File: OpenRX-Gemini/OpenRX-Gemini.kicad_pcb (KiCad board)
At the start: 6 copper layers, 13.8 x 13.7 mm, 67 parts, among them T1 0900PC16J0042001E, T2 0900PC16J0042001E, U1 ESP32-C3FH4, U10 RFX2401C, U11 SKY13588-460LF, U2 TLV75533PDQNR, U3 TS2306A 240GF MSM 9_C2976675, U4 LR1121IMLTRT, U5 OW7EL89CENUYO3YLC-32M, U6 SKY13588-460LF, U7 RFX2401C, U8 OW7EL89CENUYO3YLC-32M, U9 LR1121IMLTRT, X1 CJ17-400001010B20

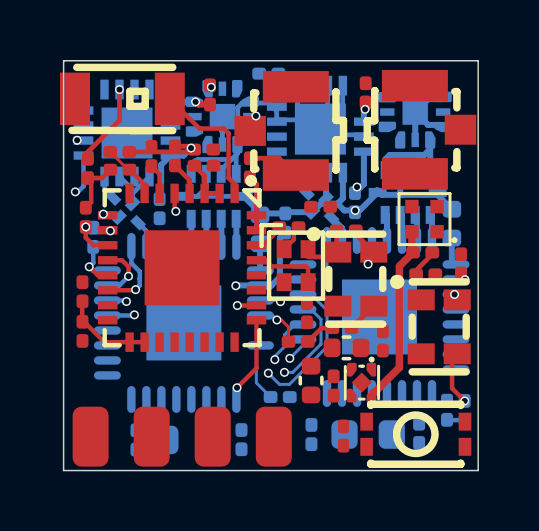
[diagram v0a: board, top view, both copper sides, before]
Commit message: Standardize repo: .gitignore, README, license, remove production from tracking
- Standardize .gitignore to match ecosystem template
- Add license section to README
- Replace LICENSE stub with full CERN-OHL-S-2.0 text
- Remove production/ from git tracking (generated, re-exportable)
- Remove tracked iCloud artifacts (.history 2 files)

Co-Authored-By: Claude Opus 4.6 (1M context) <noreply@anthropic.com>
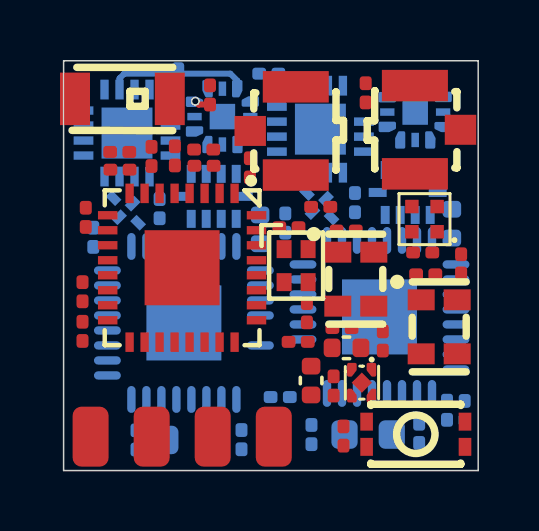
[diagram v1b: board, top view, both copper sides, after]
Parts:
- C16: moved to B.Cu
- moved C16 4.24 mm to (65.3, 45.3)
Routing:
- net GND: track 41.1 -> 0.00 mm, vias 2 -> 0
- net +3V3: track 21.3 -> 0.54 mm, vias 7 -> 1
- net +5V: track 6.05 -> 0.00 mm
- net /ESP32-C3 + 2x LR1121 Gemini/MOSI: track 5.67 -> 0.00 mm, vias 3 -> 0
- net /ESP32-C3 + 2x LR1121 Gemini/WIFI: track 4.52 -> 0.00 mm
- net /ESP32-C3 + 2x LR1121 Gemini/MISO: track 4.18 -> 0.00 mm, vias 3 -> 0
- net Net-(T1-RX): track 3.94 -> 0.00 mm
- net Net-(T2-RX): track 3.92 -> 0.00 mm
- net /ESP32-C3 + 2x LR1121 Gemini/BUSY2: track 2.55 -> 0.00 mm, vias 1 -> 0
- net /ESP32-C3 + 2x LR1121 Gemini/IRQ2: track 2.52 -> 0.00 mm, vias 1 -> 0
- net /ESP32-C3 + 2x LR1121 Gemini/XTAL_N: track 2.29 -> 0.00 mm
- net Net-(U4-VTCXO): track 2.13 -> 0.00 mm, vias 2 -> 0
- net /ESP32-C3 + 2x LR1121 Gemini/NSS2: track 2.11 -> 0.00 mm, vias 1 -> 0
- net Net-(U6-J2): track 2.75 -> 4.73 mm, vias 1 -> 0
- net /ESP32-C3 + 2x LR1121 Gemini/RST2: track 1.97 -> 0.00 mm
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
